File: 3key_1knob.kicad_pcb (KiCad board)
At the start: 2 copper layers, 99.2 x 35 mm, 17 parts, among them SW1 RotaryEncoder_Switch, U4 Kailh_socket_MX, U5 Kailh_socket_MX, U6 Kailh_socket_MX

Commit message: Route signals and power
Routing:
- net +5V: track 0.00 -> 117.2 mm
- net /KEY4: track 0.00 -> 114.6 mm
- net /CW: track 0.00 -> 101.5 mm
- net /CCW: track 0.00 -> 96.4 mm
- net /D+: track 0.00 -> 60.9 mm
- net /D-: track 0.00 -> 56.8 mm, vias 0 -> 2
- net Net-(D3-DIN): track 0.00 -> 41.3 mm, vias 0 -> 1
- net Net-(D2-DIN): track 0.00 -> 31.4 mm
- net Net-(D1-DIN): track 0.00 -> 29.3 mm
- net /KEY3: track 0.00 -> 29.0 mm
- net /KEY1: track 0.00 -> 28.9 mm
- net /KEY2: track 0.00 -> 10.3 mm
- net +3V3: track 0.00 -> 4.75 mm
- net Net-(R1-Pad2): track 0.00 -> 2.00 mm
- net /LED_DO: track 0.00 -> 2.00 mm

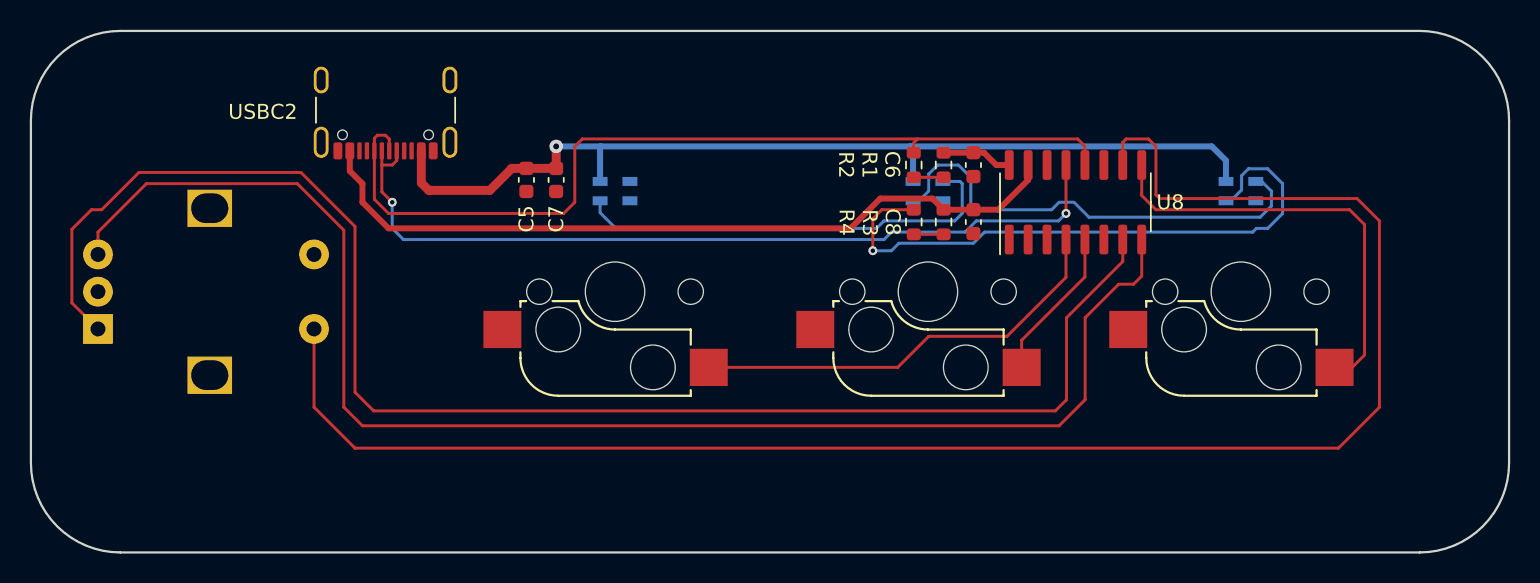
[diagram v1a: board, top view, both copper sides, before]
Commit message: Finish ground fills; Add 2 pin header; Update 3D models
This completes the PCB drawing based off the (questionable) original
design. Due to odd signal routing, there are several ground fill islands
that had to be addressed by placing microvias.

Note that with JLCPCB DRC constraints, there will be some spacing
violations due to the USBC footprint used. The USBC footprint has 2
mounting holes which are too close to power pads.

This also hides R2 resistor 3D model and displays 16-SOIC-3.9x9.9mm 3D
model. For reference, R2 is unconnected, and 16-SOP-3.9x9.9mm lacks a 3D
model so I used 16-SOIC variant instead.
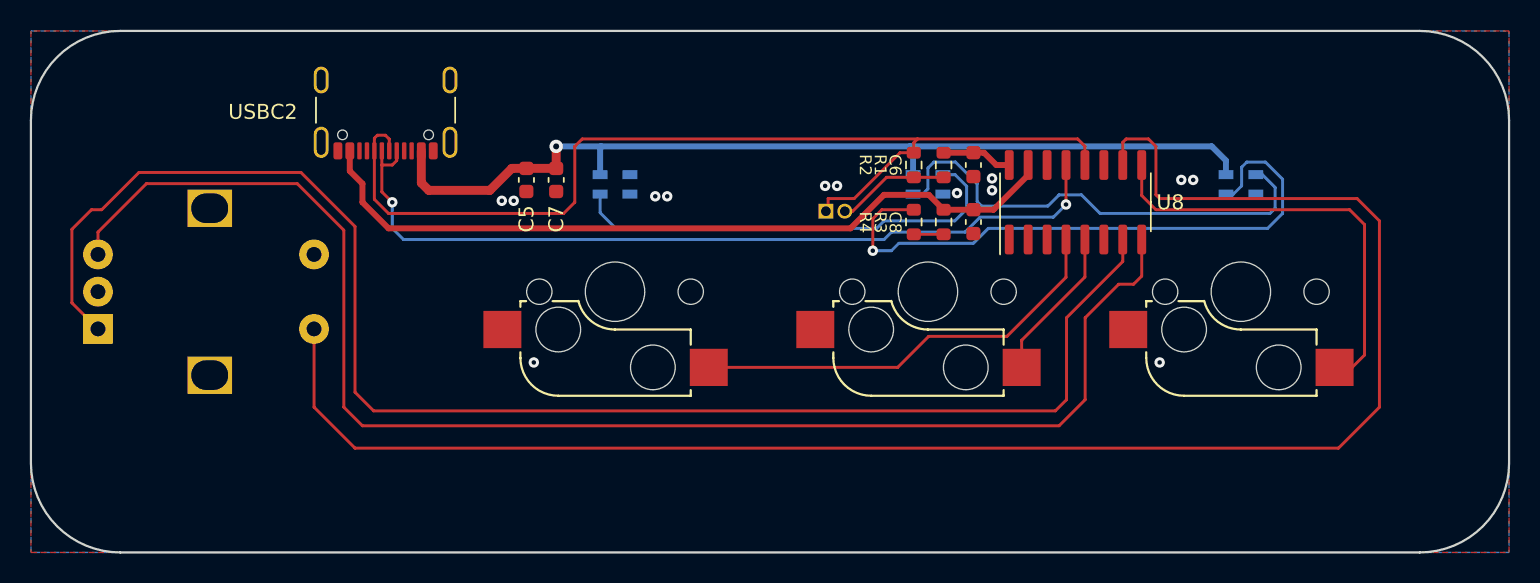
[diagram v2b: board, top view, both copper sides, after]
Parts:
- added J1: Conn_01x02, Connector_PinHeader_1.27mm:PinHeader_1x02_P1.27mm_Vertical, B.Cu at (153.3, 112.1)
- moved D1 0.45 mm to (139.2, 110.3)
- moved D2 0.45 mm to (160.2, 110.3)
- moved D3 0.45 mm to (181.2, 110.3)
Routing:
- net /D+: track 60.9 -> 68.9 mm
- net Net-(J1-Pin_2): track 2.00 -> 7.57 mm
- net +5V: track 117.2 -> 115.9 mm
- net Net-(D1-DIN): track 29.3 -> 30.3 mm
- net Net-(D2-DIN): track 31.4 -> 32.0 mm
- net Net-(D3-DIN): track 41.3 -> 41.9 mm
- net GND: vias 0 -> 13
- added copper zone on B.Cu, net GND
- added copper zone on F.Cu, net GND

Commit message: Route LED_DO signal to MCU; Adjust trace thickness and ground fills
This routes LED_DO which was previously unconnected to MCU, as well as
increase trace thickness and use thermal relief pad connections on
bottom ground fills.

Thickness of power traces decreased to 0.5.

Thickness of signal traces increased to 0.3.
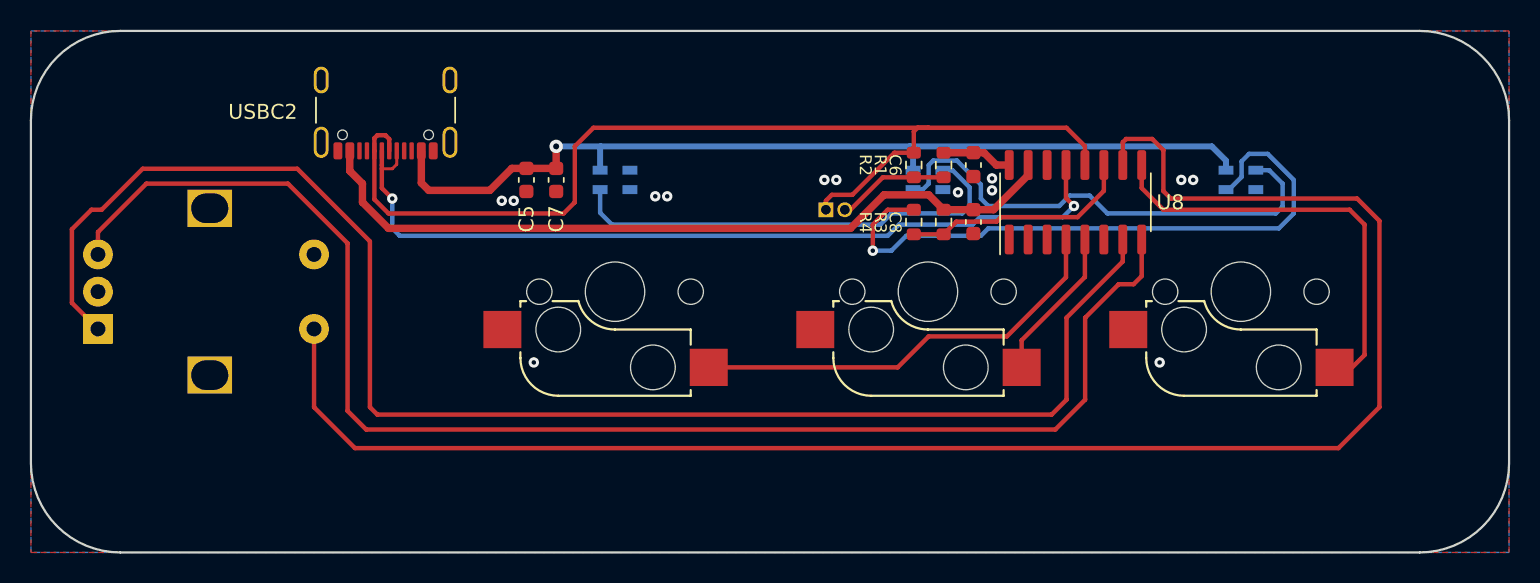
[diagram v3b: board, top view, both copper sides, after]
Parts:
- moved D1 0.30 mm to (139.2, 110.0)
- moved D2 0.30 mm to (160.2, 110.0)
- moved D3 0.30 mm to (181.2, 110.0)
- moved J1 0.10 mm to (153.3, 112.0)
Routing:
- net /LED_DO: track 2.00 -> 15.7 mm
- net /D+: track 68.9 -> 71.1 mm
- net Net-(D3-DIN): track 41.9 -> 43.3 mm
- net +5V: track 115.9 -> 115.0 mm
- net Net-(D2-DIN): track 32.0 -> 32.8 mm
- net /D-: track 56.4 -> 57.3 mm

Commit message: Minor PCB update
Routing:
- net /CW: track 101.9 -> 103.1 mm
- net /CCW: track 96.3 -> 96.9 mm
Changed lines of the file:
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@@
   (segment (start 123.55 110.55) (end 123.55 109.25) (width 0.3) (layer "F.Cu") (net 9))
   (segment (start 170 111.75) (end 169.465 111.215) (width 0.3) (layer "F.Cu") (net 9))
-  (segment (start 124.55 108.95) (end 124.25 109.25) (width 0.2) (layer "F.Cu") (net 9))
-  (segment (start 124.55 108.049487) (end 124.55 108.95) (width 0.2) (layer "F.Cu") (net 9))
+  (segment (start 124.55 108.95) (end 124.25 109.25) (width 0.3) (layer "F.Cu") (net 9))
+  (segment (start 124.55 108.049487) (end 124.55 108.95) (width 0.3) (layer "F.Cu") (net 9))
   (segment (start 123.55 108.049487) (end 123.55 109) (width 0.3) (layer "F.Cu") (net 9))
   (segment (start 124.25 111.25) (end 123.55 110.55) (width 0.3) (layer "F.Cu") (net 9))
-  (segment (start 124.25 109.25) (end 123.55 109.25) (width 0.2) (layer "F.Cu") (net 9))
+  (segment (start 124.25 109.25) (end 123.55 109.25) (width 0.3) (layer "F.Cu") (net 9))
   (segment (start 169.465 111.215) (end 169.465 109) (width 0.3) (layer "F.Cu") (net 9))
   (segment (start 123.55 109.25) (end 123.55 109) (width 0.3) (layer "F.Cu") (net 9))
@@
   (segment (start 162.1 112.8) (end 164.798946 112.8) (width 0.3) (layer "F.Cu") (net 10))
   (segment (start 170.23995 112.5) (end 172.005 110.73495) (width 0.3) (layer "F.Cu") (net 10))
+  (segment (start 104.75 112) (end 108 108.75) (width 0.3) (layer "F.Cu") (net 11))
+  (segment (start 108 108.75) (end 117.375 108.75) (width 0.3) (layer "F.Cu") (net 11))
+  (segment (start 102.25 117.75) (end 102.25 113.25) (width 0.3) (layer "F.Cu") (net 11))
+  (segment (start 104.5 120) (end 102.25 117.75) (width 0.3) (layer "F.Cu") (net 11))
+  (segment (start 122.75 114.125) (end 122.75 125.25) (width 0.3) (layer "F.Cu") (net 11))
+  (segment (start 102.25 113.25) (end 103.5 112) (width 0.3) (layer "F.Cu") (net 11))
   (segment (start 173.275 115.475) (end 173.275 114) (width 0.3) (layer "F.Cu") (net 11))
-  (segment (start 117.875 109.25) (end 122.75 114.125) (width 0.3) (layer "F.Cu") (net 11))
+  (segment (start 103.5 112) (end 104.75 112) (width 0.3) (layer "F.Cu") (net 11))
+  (segment (start 169.5 119.25) (end 173.275 115.475) (width 0.3) (layer "F.Cu") (net 11))
+  (segment (start 122.75 125.25) (end 123.25 125.75) (width 0.3) (layer "F.Cu") (net 11))
+  (segment (start 169.5 124.75) (end 169.5 119.25) (width 0.3) (layer "F.Cu") (net 11))
   (segment (start 168.5 125.75) (end 169.5 124.75) (width 0.3) (layer "F.Cu") (net 11))
-  (segment (start 102.75 113.3125) (end 104.0625 112) (width 0.3) (layer "F.Cu") (net 11))
-  (segment (start 104.0625 112) (end 104.75 112) (width 0.3) (layer "F.Cu") (net 11))
   (segment (start 123.25 125.75) (end 168.5 125.75) (width 0.3) (layer "F.Cu") (net 11))
-  (segment (start 104.75 112) (end 107.5 109.25) (width 0.3) (layer "F.Cu") (net 11))
-  (segment (start 104.5 120) (end 102.75 118.25) (width 0.3) (layer "F.Cu") (net 11))
-  (segment (start 122.75 114.125) (end 122.75 125.25) (width 0.3) (layer "F.Cu") (net 11))
-  (segment (start 169.5 124.75) (end 169.5 119.25) (width 0.3) (layer "F.Cu") (net 11))
-  (segment (start 122.75 125.25) (end 123.25 125.75) (width 0.3) (layer "F.Cu") (net 11))
-  (segment (start 102.75 118.25) (end 102.75 113.3125) (width 0.3) (layer "F.Cu") (net 11))
-  (segment (start 169.5 119.25) (end 173.275 115.475) (width 0.3) (layer "F.Cu") (net 11))
-  (segment (start 107.5 109.25) (end 117.875 109.25) (width 0.3) (layer "F.Cu") (net 11))
+  (segment (start 117.375 108.75) (end 122.75 114.125) (width 0.3) (layer "F.Cu") (net 11))
+  (segment (start 104.5 115) (end 104.5 113.5) (width 0.3) (layer "F.Cu") (net 12))
+  (segment (start 108.5 109.5) (end 116.5 109.5) (width 0.3) (layer "F.Cu") (net 12))
+  (segment (start 170.75 119.25) (end 173 117) (width 0.3) (layer "F.Cu") (net 12))
+  (segment (start 173 117) (end 174 117) (width 0.3) (layer "F.Cu") (net 12))
+  (segment (start 174 117) (end 174.545 116.455) (width 0.3) (layer "F.Cu") (net 12))
+  (segment (start 122.5 126.75) (end 168.75 126.75) (width 0.3) (layer "F.Cu") (net 12))
+  (segment (start 174.545 116.455) (end 174.545 114) (width 0.3) (layer "F.Cu") (net 12))
   (segment (start 121.25 114.25) (end 121.25 125.5) (width 0.3) (layer "F.Cu") (net 12))
-  (segment (start 104.5 115) (end 104.5 113.5) (width 0.3) (layer "F.Cu") (net 12))
+  (segment (start 104.5 113.5) (end 108.5 109.5) (width 0.3) (layer "F.Cu") (net 12))
+  (segment (start 116.5 109.5) (end 121.25 114.25) (width 0.3) (layer "F.Cu") (net 12))
+  (segment (start 170.75 124.75) (end 170.75 119.25) (width 0.3) (layer "F.Cu") (net 12))
+  (segment (start 168.75 126.75) (end 170.75 124.75) (width 0.3) (layer "F.Cu") (net 12))
   (segment (start 121.25 125.5) (end 122.5 126.75) (width 0.3) (layer "F.Cu") (net 12))
-  (segment (start 107.75 110.25) (end 117.25 110.25) (width 0.3) (layer "F.Cu") (net 12))
-  (segment (start 104.5 113.5) (end 107.75 110.25) (width 0.3) (layer "F.Cu") (net 12))
-  (segment (start 174 117) (end 174.545 116.455) (width 0.3) (layer "F.Cu") (net 12))
-  (segment (start 174.545 116.455) (end 174.545 114) (width 0.3) (layer "F.Cu") (net 12))
-  (segment (start 170.75 124.75) (end 170.75 119.25) (width 0.3) (layer "F.Cu") (net 12))
-  (segment (start 122.5 126.75) (end 168.75 126.75) (width 0.3) (layer "F.Cu") (net 12))
-  (segment (start 173 117) (end 174 117) (width 0.3) (layer "F.Cu") (net 12))
-  (segment (start 117.25 110.25) (end 121.25 114.25) (width 0.3) (layer "F.Cu") (net 12))
-  (segment (start 170.75 119.25) (end 173 117) (width 0.3) (layer "F.Cu") (net 12))
-  (segment (start 168.75 126.75) (end 170.75 124.75) (width 0.3) (layer "F.Cu") (net 12))
   (segment (start 190.5 112.75) (end 190.5 125.25) (width 0.3) (layer "F.Cu") (net 13))
   (segment (start 119 125.25) (end 119 120) (width 0.3) (layer "F.Cu") (net 13))

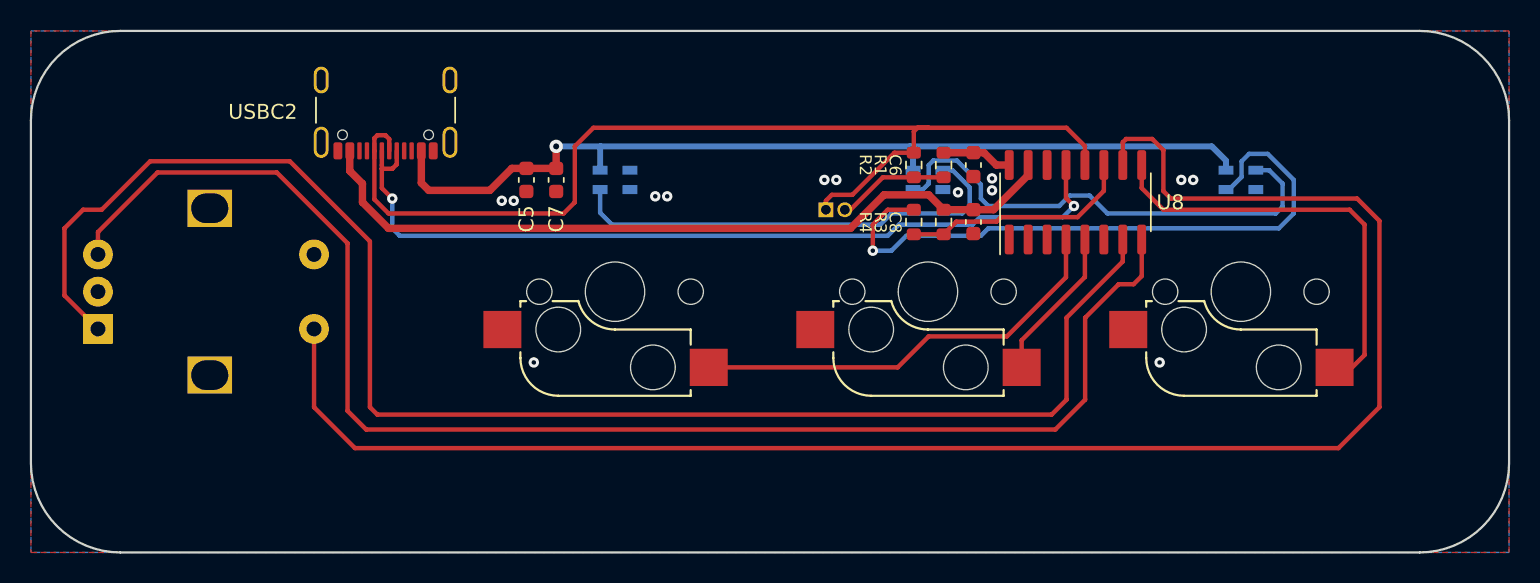
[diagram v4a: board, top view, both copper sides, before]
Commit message: Adjust LED positions and traces for better accuracy
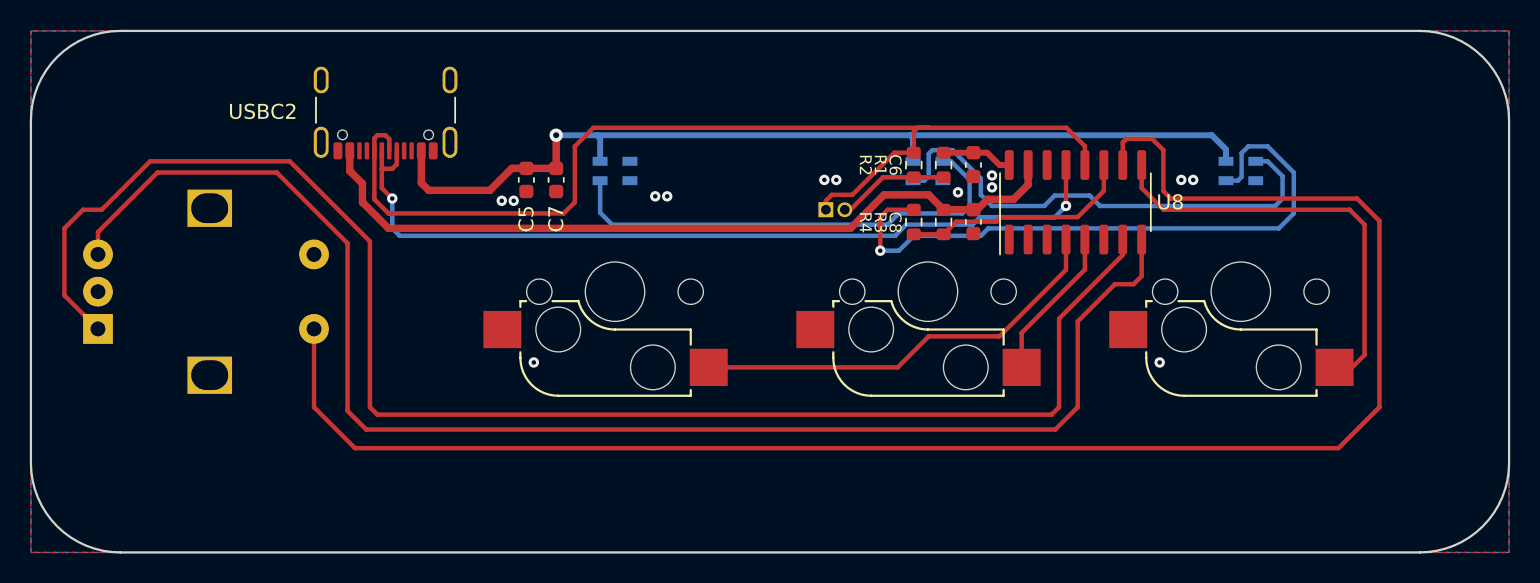
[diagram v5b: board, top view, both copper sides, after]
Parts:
- moved D1 0.60 mm to (139.2, 109.4)
- moved D2 0.60 mm to (160.2, 109.4)
- moved D3 0.60 mm to (181.2, 109.4)
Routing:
- net +5V: track 115.0 -> 116.6 mm
- net Net-(D1-DIN): track 30.7 -> 31.9 mm
- net /D-: track 57.3 -> 56.5 mm
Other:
- board text added: "Subsituted components (unable to find original BOM): - USBC receptacle - RGB LED - Key switch socket"
- board text added: "USBC Micropad with 3 Hotswappable Key Switches, 1 Rotary Encoder (Knob), and 3 Addressable RGB LEDs."

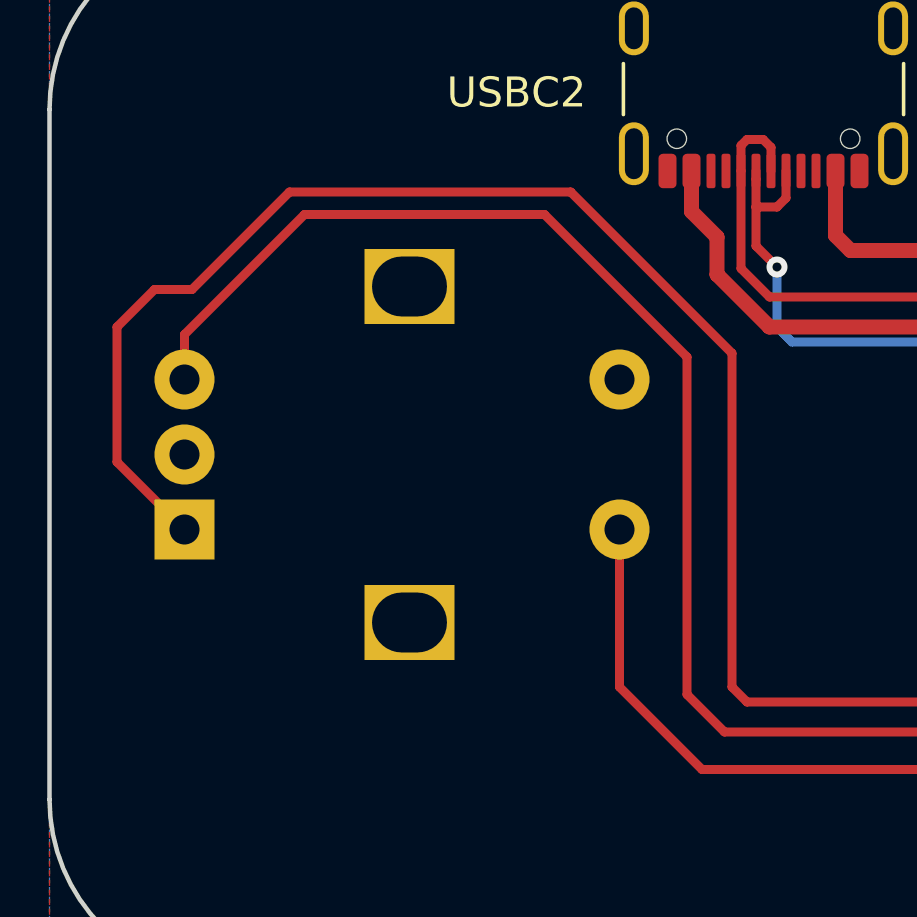
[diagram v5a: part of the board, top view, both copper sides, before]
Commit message: Connect USBC receptacle and Rotary Encoder shield to ground; Adjust traces
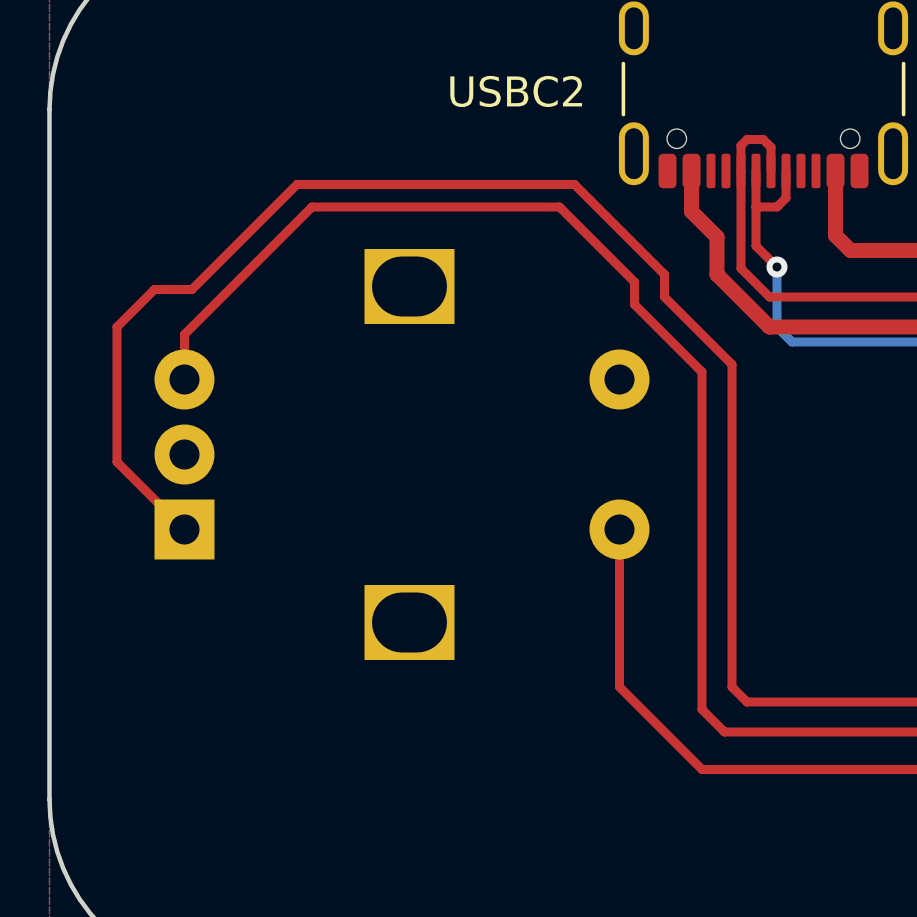
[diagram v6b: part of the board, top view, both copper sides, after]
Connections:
- SW1 pad MP: (no net) -> GND
- USBC2 pad S1: unconnected-(USBC2-SHIELD-PadS1) -> GND
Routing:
- net /CCW: track 97.0 -> 97.7 mm
